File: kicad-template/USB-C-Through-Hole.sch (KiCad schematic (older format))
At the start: 4 parts

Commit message: working on adding support for jlcpcb small batch assembly
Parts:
- ESD1: LCSC (none) -> C12333
- R6: LCSC (none) -> C122969; MPN RR0816P-512-D -> RT0603BRD075K1L; Manufacturer Susumu -> Yaego
- R7: DigiKey RR08P5.1KDTR-ND -> (none); LCSC (none) -> C122969; MPN RR0816P-512-D -> RT0603BRD075K1L; Manufacturer Susumu -> Yaego
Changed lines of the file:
@@
 F 1 "5.1K" V 3907 5351 40  0000 C CNN
 F 2 "Resistor_SMD:R_0603_1608Metric" V 3830 5350 30  0001 C CNN
-F 3 "http://www.susumu.co.jp/common/pdf/n_catalog_partition05_en.pdf" H 3900 5350 30  0001 C CNN
-F 4 "RR0816P-512-D" V 3900 5350 50  0001 C CNN "MPN"
+F 3 "" H 3900 5350 30  0001 C CNN
+F 4 "RT0603BRD075K1L" V 3900 5350 50  0001 C CNN "MPN"
 F 5 "RES SMD 5.1K OHM 0.5% 1/16W 0603" H -5700 275 50  0001 C CNN "Description"
-F 6 "RR08P5.1KDTR-ND" H -5700 275 50  0001 C CNN "DigiKey"
-F 7 "Susumu" H -5700 275 50  0001 C CNN "Manufacturer"
+F 6 "" H -5700 275 50  0001 C CNN "DigiKey"
+F 7 "Yaego" H -5700 275 50  0001 C CNN "Manufacturer"
 F 8 "RT0603BRD075K1L	" H 0   0   50  0001 C CNN "Seeed Part Num"
+F 9 "C122969" V 3900 5350 50  0001 C CNN "LCSC"
 	1    3900 5350
 	0    -1   -1   0
@@
 F 1 "5.1K" V 3907 5101 40  0000 C CNN
 F 2 "Resistor_SMD:R_0603_1608Metric" V 3830 5100 30  0001 C CNN
-F 3 "http://www.susumu.co.jp/common/pdf/n_catalog_partition05_en.pdf" H 3900 5100 30  0001 C CNN
-F 4 "RR0816P-512-D" V 3900 5100 50  0001 C CNN "MPN"
+F 3 "" H 3900 5100 30  0001 C CNN
+F 4 "RT0603BRD075K1L" V 3900 5100 50  0001 C CNN "MPN"
 F 5 "RES SMD 5.1K OHM 0.5% 1/16W 0603" H -5450 25  50  0001 C CNN "Description"
 F 6 "RR08P5.1KDTR-ND" H -5450 25  50  0001 C CNN "DigiKey"
-F 7 "Susumu" H -5450 25  50  0001 C CNN "Manufacturer"
+F 7 "Yaego" H -5450 25  50  0001 C CNN "Manufacturer"
 F 8 "RT0603BRD075K1L	" H 0   0   50  0001 C CNN "Seeed Part Num"
+F 9 "C122969" V 3900 5100 50  0001 C CNN "LCSC"
 	1    3900 5100
 	0    -1   -1   0
@@
 F 7 "Nexperia" H -2925 -125 50  0001 C CNN "Manufacturer"
 F 8 "PRTR5V0U2X,215	" H 0   0   50  0001 C CNN "Seeed Part Num"
+F 9 "C12333" H 1875 5025 50  0001 C CNN "LCSC"
 	1    1875 5025
 	1    0    0    -1

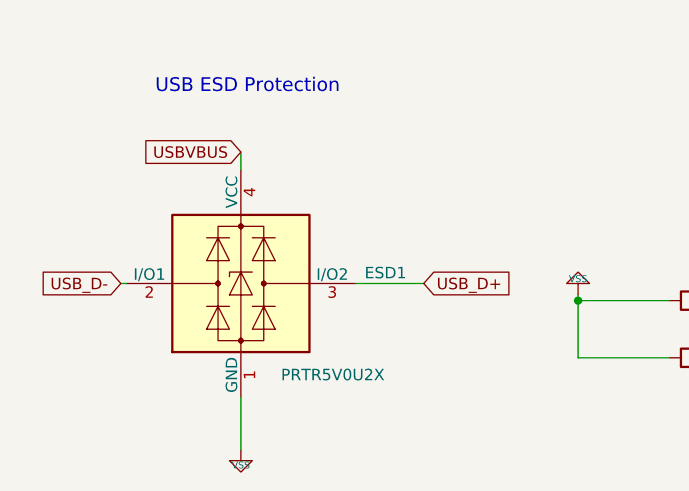
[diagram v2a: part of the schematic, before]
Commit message: Trying to get back to Kicad 5.1 compat and fix USB routing
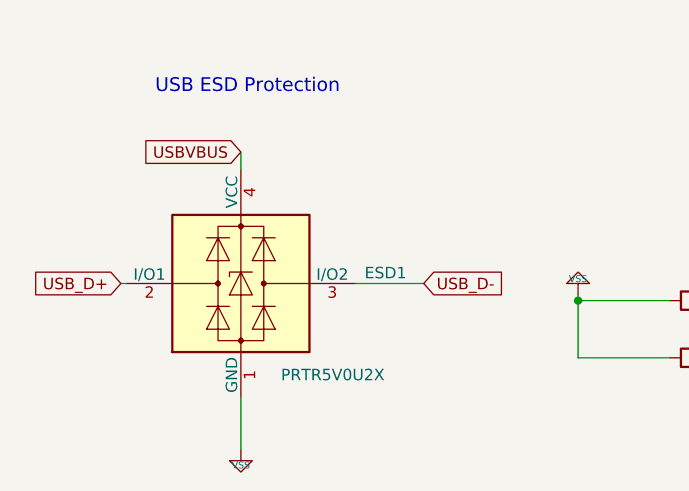
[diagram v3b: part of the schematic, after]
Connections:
- net USB_D+: now also ESD1.2 (I/O1); no longer ESD1.3 (I/O2)
- net USB_D-: now also ESD1.3 (I/O2); no longer ESD1.2 (I/O1)
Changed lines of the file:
@@
-EESchema Schematic File Version 5
+EESchema Schematic File Version 4
 LIBS:kicad-template-cache
 EELAYER 30 0
@@
 Comment3 ""
 Comment4 ""
-Comment5 ""
-Comment6 ""
-Comment7 ""
-Comment8 ""
-Comment9 ""
 $EndDescr
 $Comp
@@
 USBGND
 Text GLabel 2675 5025 2    50   Input ~ 0
+USB_D-
+Text GLabel 1350 5025 0    50   Input ~ 0
 USB_D+
-Text GLabel 1350 5025 0    50   Input ~ 0
-USB_D-
 Text Notes 7525 2050 0    197  ~ 39
 USB Support Circuitry
@@
 U 1 1 5CA6A220
 P 1875 5750
-AR Path="/5CA54797/5CA6A220" Ref="#PWR?"  Part="1"
-AR Path="/5B90A59E/5CA5B11A/5CA6A220" Ref="#PWR?"  Part="1"
-AR Path="/5B90A59F/5CA5B290/5CA6A220" Ref="#PWR?"  Part="1"
-AR Path="/5B90A59E/5CA6A220" Ref="#PWR?"  Part="1"
-AR Path="/5B90A59F/5CA6A220" Ref="#PWR?"  Part="1"
-AR Path="/5CA6A220" Ref="#PWR?"  Part="1"
-AR Path="/5D950BDF/5CA6A220" Ref="#PWR?"  Part="1"
 F 0 "#PWR?" H 1875 5750 30  0001 C CNN
 F 1 "VSS" H 1875 5680 30  0000 C CNN
@@
 U 1 1 5CA6A217
 P 1875 5025
-AR Path="/5CA54797/5CA6A217" Ref="ESD1"  Part="1"
-AR Path="/5B90A59E/5CA5B11A/5CA6A217" Ref="ESD1"  Part="1"
-AR Path="/5B90A59F/5CA5B290/5CA6A217" Ref="ESD1"  Part="1"
-AR Path="/5B90A59E/5CA6A217" Ref="ESD1"  Part="1"
-AR Path="/5B90A59F/5CA6A217" Ref="ESD1"  Part="1"
-AR Path="/5CA6A217" Ref="ESD1"  Part="1"
-AR Path="/5D950BDF/5CA6A217" Ref="ESD1"  Part="1"
 F 0 "ESD1" H 2416 5071 50  0000 L CNN
 F 1 "PRTR5V0U2X" H 2050 4625 50  0000 L CNN
